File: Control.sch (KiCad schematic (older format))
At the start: 25 parts, among them J3 PDI, U6 ADR380, U7 ATXMEGA32E5-AU

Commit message: First working version
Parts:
- removed DS1: CV, smd-semi:LED-0603, symbol LED-0603
- removed DS2: CC, smd-semi:LED-0603, symbol LED-0603
- removed R52: 20k, IPC7351-Nominal:RESC1608X50, symbol R-0603
- removed W3: NET-TIE, conn-test:NET-TIE-1mm, symbol NET-TIE
- added C52, C53: 100n, IPC7351-Nominal:CAPC1608X55, symbol C-0603
- added DS1: CV, pth-semi:LED-5mm, symbol LED-5MM
- added DS2: CC, pth-semi:LED-5mm, symbol LED-5MM
- added J7: BUTTONS, conn-100mil:CONN-100MIL-M-1x3-SHROUD, symbol CONN-100MIL-M-1x3-SHROUD
- added U4: MCP9701-E/TO, conn-100mil:CONN-100MIL-M-1x3, symbol MCP9701-E/TO
- R32, R33, R56: value 330 -> 348; BOM RES SMD 330 1% [0603] -> RES SMD 348 1% [0603]
- R34, R50, R53: value 20k -> 22k; BOM RES SMD 20k 1% [0603] -> RES SMD 22k 1% [0603]
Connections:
- net labels added: PWR, TEMP, ~EN, ~ILIM, ~VLIM
- net labels removed: ILIM, VLIM
- wire segments 85 -> 99
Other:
- note added: "Ratio: 1/12"
- moved on the sheet: C20, C21, C51, R32, R33, R50, R51, R54, R55

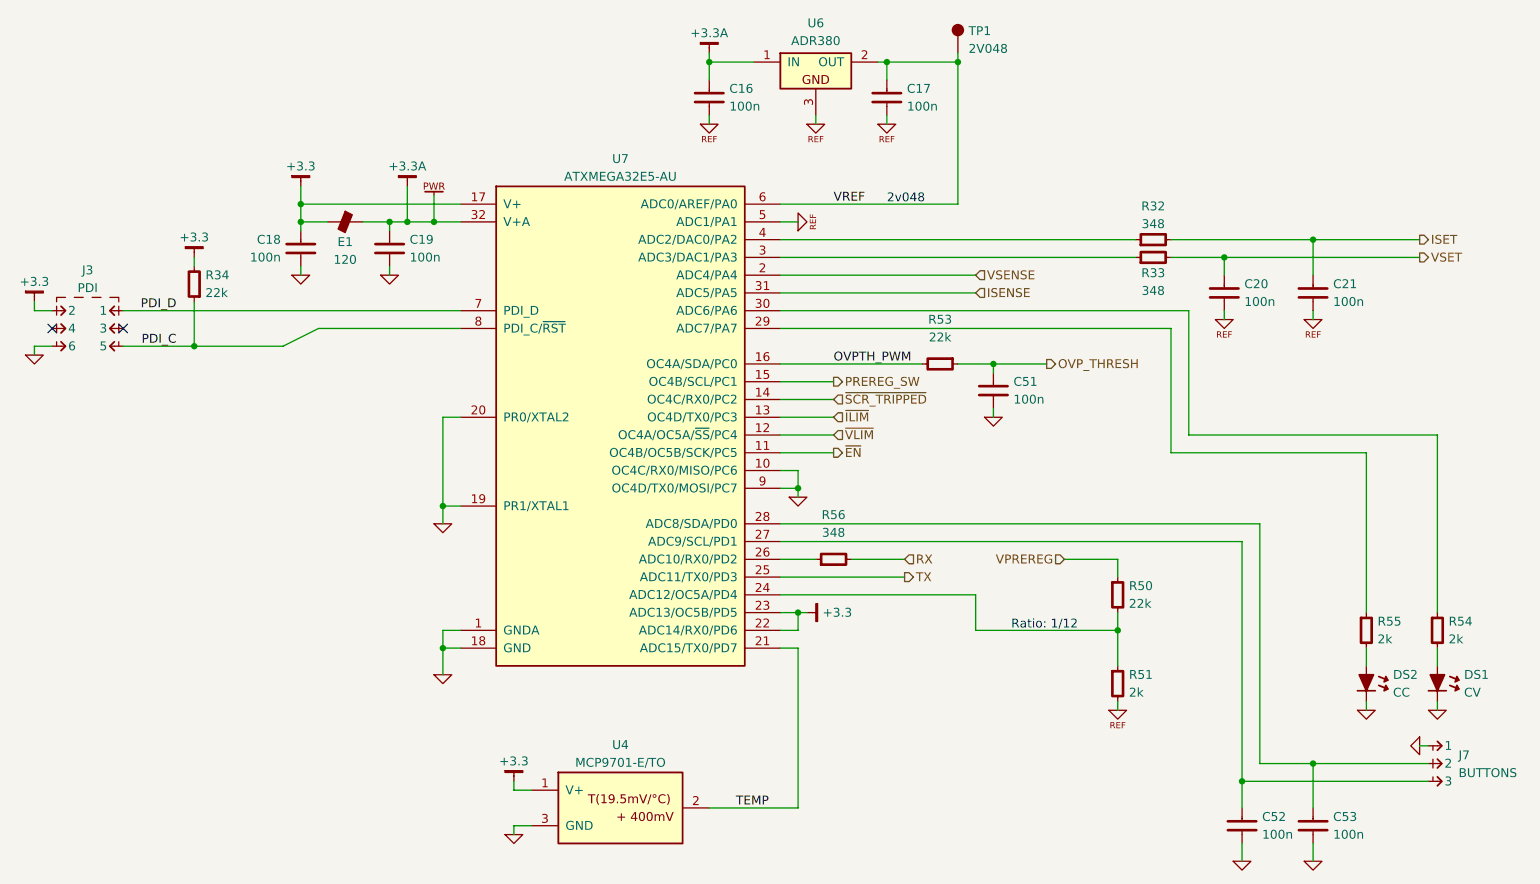
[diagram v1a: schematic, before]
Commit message: Reannotate component references
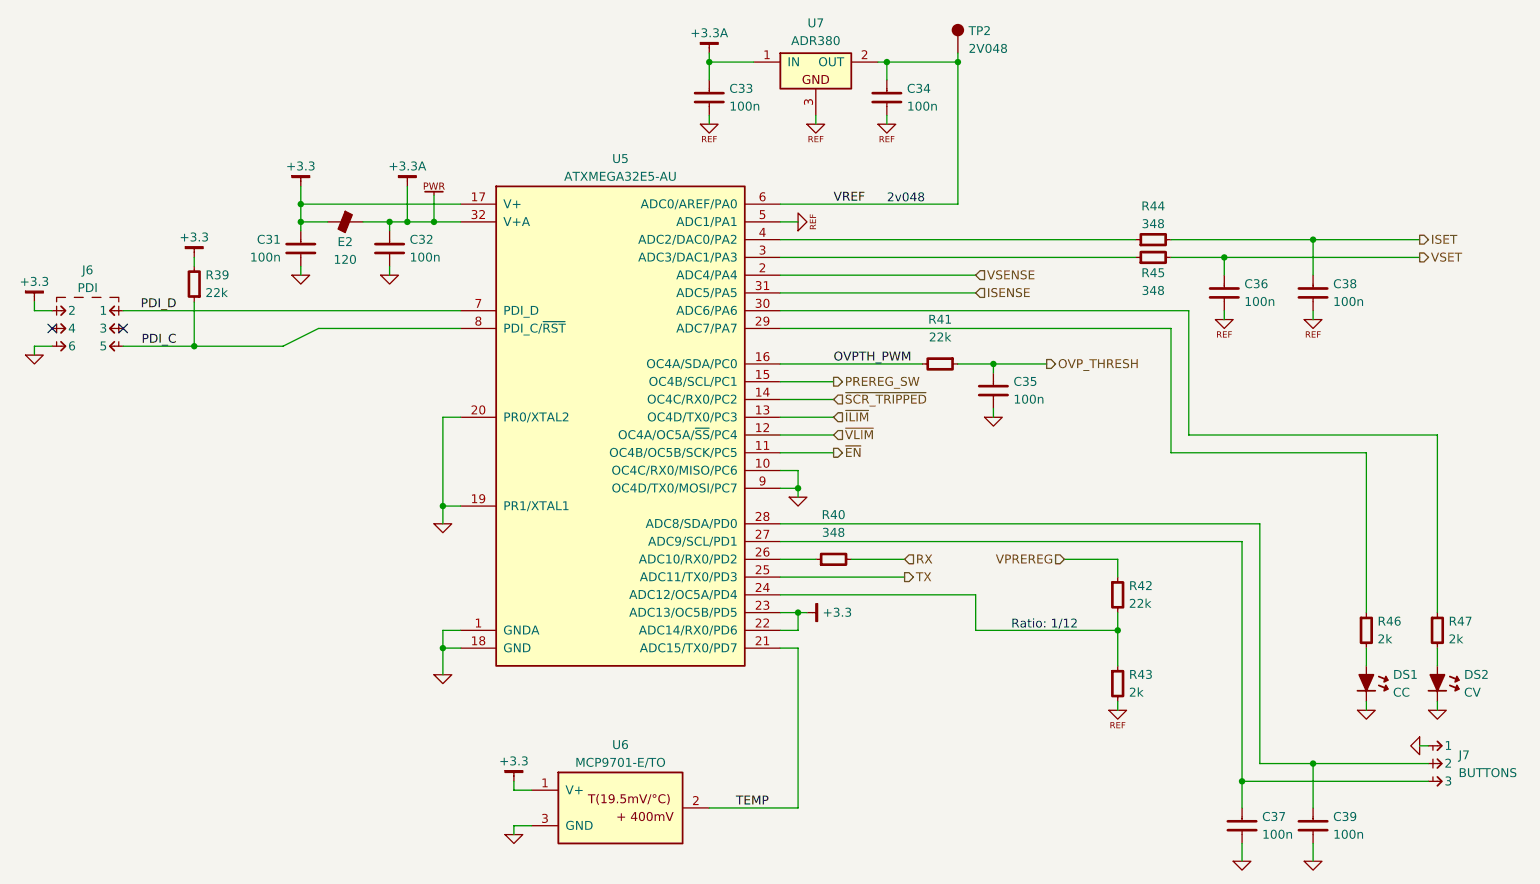
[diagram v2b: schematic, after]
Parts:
- renumbered C18 to C31, C19 to C32, C16 to C33, C17 to C34, C51 to C35, C20 to C36, C52 to C37, C21 to C38, C53 to C39, DS2 to DS1, DS1 to DS2, E1 to E2, J3 to J6, R34 to R39, R56 to R40, R53 to R41, R50 to R42, R51 to R43, R32 to R44, R33 to R45, R55 to R46, R54 to R47, TP1 to TP2, U7 to U5, U4 to U6, U6 to U7

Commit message: Piles and piles of work
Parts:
- removed R40: 348, IPC7351-Nominal:RESC1608X50, symbol R-0603
- removed U5: ATXMEGA32E5-AU, IPC7351-Nominal:QFP80P900X900X120-32, symbol ATXMEGA32E5-AU
- added U5: ATXMEGA8E5-AU, IPC7351-Nominal:QFP80P900X900X120-32, symbol ATXMEGA8E5-AU
- J6: BOM (none) -> (6) PIN STRIP 100mil
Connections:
- net +3.3: now also U5.17 (V+), U5.22 (ADC14/RX0/PD6), U5.23 (ADC13/OC5B/PD5)
- net +3.3A: now also U5.32 (V+A)
- net GND: now also U5.1 (GNDA), U5.10 (OC4C/RX0/MISO/PC6), U5.18 (GND), U5.19 (PR1/XTAL1), U5.20 (PR0/XTAL2), U5.9 (OC4D/TX0/MOSI/PC7)
- net ISENSE: now also U5.31 (ADC5/PA5)
- net OVPTH_PWM: now also U5.16 (OC4A/SDA/PC0)
- net PDI_C: now also U5.8 (PDI_C/~RST)
- net PDI_D: now also U5.7 (PDI_D)
- net PREREG_SW: now also U5.15 (OC4B/SCL/PC1)
- net REFGND: now also U5.5 (ADC1/PA1)
- net RX: now also U5.26 (ADC10/RX0/PD2)
- net TEMP: now also U5.21 (ADC15/TX0/PD7)
- net TX: now also U5.25 (ADC11/TX0/PD3)
- net VREF: now also U5.6 (ADC0/AREF/PA0)
- net VSENSE: now also U5.2 (ADC4/PA4)
- net ~EN: now also U5.11 (OC4B/OC5B/SCK/PC5)
- net ~ILIM: now also U5.13 (OC4D/TX0/PC3)
- net ~SCR_TRIPPED: now also U5.14 (OC4C/RX0/PC2)
- net ~VLIM: now also U5.12 (OC4A/OC5A/~SS~/PC4)
- net at R42.2, R43.1: now also U5.24 (ADC12/OC5A/PD4)
- net at C37.2, J7.3: now also U5.27 (ADC9/SCL/PD1)
- net at C39.2, J7.2: now also U5.28 (ADC8/SDA/PD0)
- net at R46.1: now also U5.29 (ADC7/PA7)
- net at R45.1: now also U5.3 (ADC3/DAC1/PA3)
- net at R47.1: now also U5.30 (ADC6/PA6)
- net at R44.1: now also U5.4 (ADC2/DAC0/PA2)
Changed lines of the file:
@@
 $EndDescr
 $Comp
-L ATXMEGA32E5-AU U5
-U 1 1 55CC4ECA
-P 4500 3950
-F 0 "U5" H 4500 5455 50  0000 C CNN
-F 1 "ATXMEGA32E5-AU" H 4500 5355 50  0000 C CNN
-F 2 "IPC7351-Nominal:QFP80P900X900X120-32" H 4500 2550 50  0001 C CNN
-F 3 "" H 4200 4300 50  0000 C CNN
-F 4 "IC ATMEL ATXMEGA32E5-AU" H 4500 2450 50  0001 C CNN "BOM"
-	1    4500 3950
-	1    0    0    -1
-$EndComp
-$Comp
-L +3.3 #PWR67
+L +3.3 #PWR66
 U 1 1 55CC5274
 P 2700 2600
-F 0 "#PWR67" H 2700 2650 30  0001 C CNN
+F 0 "#PWR66" H 2700 2650 30  0001 C CNN
 F 1 "+3.3" H 2700 2713 50  0000 C CNN
 F 2 "" H 2700 2600 60  0000 C CNN
@@
 $EndComp
 $Comp
-L GND #PWR68
+L GND #PWR67
 U 1 1 55CCA52E
 P 2700 3100
-F 0 "#PWR68" H 2700 3100 30  0001 C CNN
+F 0 "#PWR67" H 2700 3100 30  0001 C CNN
 F 1 "GND" H 2700 3030 30  0001 C CNN
 F 2 "" H 2700 3100 60  0000 C CNN
@@
 $EndComp
 $Comp
-L GND #PWR73
+L GND #PWR72
 U 1 1 55CCA8CD
 P 3500 5350
-F 0 "#PWR73" H 3500 5350 30  0001 C CNN
+F 0 "#PWR72" H 3500 5350 30  0001 C CNN
 F 1 "GND" H 3500 5280 30  0001 C CNN
 F 2 "" H 3500 5350 60  0000 C CNN
@@
 $EndComp
 $Comp
-L +3.3A #PWR76
+L +3.3A #PWR75
 U 1 1 55CCD224
 P 5000 1850
-F 0 "#PWR76" H 5000 1900 30  0001 C CNN
+F 0 "#PWR75" H 5000 1900 30  0001 C CNN
 F 1 "+3.3A" H 5000 1963 50  0000 C CNN
 F 2 "" H 5000 1850 60  0000 C CNN
@@
 $EndComp
 $Comp
-L +3.3A #PWR70
+L +3.3A #PWR69
 U 1 1 55CCD672
 P 3300 2600
-F 0 "#PWR70" H 3300 2650 30  0001 C CNN
+F 0 "#PWR69" H 3300 2650 30  0001 C CNN
 F 1 "+3.3A" H 3300 2713 50  0000 C CNN
 F 2 "" H 3300 2600 60  0000 C CNN
@@
 F 2 "conn-100mil:CONN-100MIL-M-2x3" H 1475 3300 50  0001 C CNN
 F 3 "" H 1475 3300 50  0000 C CNN
+F 4 "(6) PIN STRIP 100mil" H 1500 3300 60  0001 C CNN "BOM"
 	1    1500 3300
 	-1   0    0    -1
@@
 NoConn ~ 1300 3400
 $Comp
-L +3.3 #PWR64
+L +3.3 #PWR63
 U 1 1 55CD2985
 P 1200 3250
-F 0 "#PWR64" H 1200 3300 30  0001 C CNN
+F 0 "#PWR63" H 1200 3300 30  0001 C CNN
 F 1 "+3.3" H 1200 3363 50  0000 C CNN
 F 2 "" H 1200 3250 60  0000 C CNN
@@
 $EndComp
 $Comp
-L GND #PWR65
+L GND #PWR64
 U 1 1 55CD29EB
 P 1200 3550
-F 0 "#PWR65" H 1200 3550 30  0001 C CNN
+F 0 "#PWR64" H 1200 3550 30  0001 C CNN
 F 1 "GND" H 1200 3480 30  0001 C CNN
 F 2 "" H 1200 3550 60  0000 C CNN
@@
 $EndComp
 $Comp
-L +3.3 #PWR66
+L +3.3 #PWR65
 U 1 1 55CD3055
 P 2100 3000
-F 0 "#PWR66" H 2100 3050 30  0001 C CNN
+F 0 "#PWR65" H 2100 3050 30  0001 C CNN
 F 1 "+3.3" H 2100 3113 50  0000 C CNN
 F 2 "" H 2100 3000 60  0000 C CNN
@@
 RX
 $Comp
-L REFGND #PWR82
+L REFGND #PWR81
 U 1 1 55D1DEF0
 P 6000 2250
-F 0 "#PWR82" H 6000 2250 30  0001 C CNN
+F 0 "#PWR81" H 6000 2250 30  0001 C CNN
 F 1 "REFGND" H 6000 2180 30  0001 C CNN
 F 2 "" H 6000 2250 60  0000 C CNN
@@
 $EndComp
 $Comp
-L REFGND #PWR81
+L REFGND #PWR80
 U 1 1 55D1DF25
 P 5600 2250
-F 0 "#PWR81" H 5600 2250 30  0001 C CNN
+F 0 "#PWR80" H 5600 2250 30  0001 C CNN
 F 1 "REFGND" H 5600 2180 30  0001 C CNN
 F 2 "" H 5600 2250 60  0000 C CNN
@@
 $EndComp
 $Comp
-L REFGND #PWR77
+L REFGND #PWR76
 U 1 1 55D1DF5A
 P 5000 2250
-F 0 "#PWR77" H 5000 2250 30  0001 C CNN
+F 0 "#PWR76" H 5000 2250 30  0001 C CNN
 F 1 "REFGND" H 5000 2180 30  0001 C CNN
 F 2 "" H 5000 2250 60  0000 C CNN
@@
 ISENSE
 $Comp
-L REFGND #PWR85
+L REFGND #PWR84
 U 1 1 55D23537
 P 7900 3350
-F 0 "#PWR85" H 7900 3350 30  0001 C CNN
+F 0 "#PWR84" H 7900 3350 30  0001 C CNN
 F 1 "REFGND" H 7900 3280 30  0001 C CNN
 F 2 "" H 7900 3350 60  0000 C CNN
@@
 $EndComp
 $Comp
-L REFGND #PWR87
+L REFGND #PWR86
 U 1 1 55D235A7
 P 8400 3350
-F 0 "#PWR87" H 8400 3350 30  0001 C CNN
+F 0 "#PWR86" H 8400 3350 30  0001 C CNN
 F 1 "REFGND" H 8400 3280 30  0001 C CNN
 F 2 "" H 8400 3350 60  0000 C CNN
@@
 $EndComp
 $Comp
-L REFGND #PWR84
+L REFGND #PWR83
 U 1 1 55D18E16
 P 7300 5550
-F 0 "#PWR84" H 7300 5550 30  0001 C CNN
+F 0 "#PWR83" H 7300 5550 30  0001 C CNN
 F 1 "REFGND" H 7300 5480 30  0001 C CNN
 F 2 "" H 7300 5550 60  0000 C CNN
@@
 $EndComp
 $Comp
-L GND #PWR83
+L GND #PWR82
 U 1 1 55D1B336
 P 6600 3900
-F 0 "#PWR83" H 6600 3900 30  0001 C CNN
+F 0 "#PWR82" H 6600 3900 30  0001 C CNN
 F 1 "GND" H 6600 3830 30  0001 C CNN
 F 2 "" H 6600 3900 60  0000 C CNN
@@
 $EndComp
 $Comp
-L GND #PWR91
+L GND #PWR90
 U 1 1 55D18733
 P 9100 5550
-F 0 "#PWR91" H 9100 5550 30  0001 C CNN
+F 0 "#PWR90" H 9100 5550 30  0001 C CNN
 F 1 "GND" H 9100 5480 30  0001 C CNN
 F 2 "" H 9100 5550 60  0000 C CNN
@@
 $EndComp
 $Comp
-L GND #PWR89
+L GND #PWR88
 U 1 1 55D18843
 P 8700 5550
-F 0 "#PWR89" H 8700 5550 30  0001 C CNN
+F 0 "#PWR88" H 8700 5550 30  0001 C CNN
 F 1 "GND" H 8700 5480 30  0001 C CNN
 F 2 "" H 8700 5550 60  0000 C CNN
@@
 	1    8700 5550
 	1    0    0    -1
-$EndComp
-$Comp
-L R-0603 R?
-U 1 1 55D19211
-P 5700 4700
-AR Path="/55C7FF09/55D19211" Ref="R?"  Part="1"
-AR Path="/55CDE77D/55D19211" Ref="R40"  Part="1"
-F 0 "R40" V 5950 4700 50  0000 C CNN
-F 1 "348" V 5850 4700 50  0000 C CNN
-F 2 "IPC7351-Nominal:RESC1608X50" H 5700 4700 50  0001 C CNN
-F 3 "" H 5700 4750 60  0000 C CNN
-F 4 "RES SMD 348 1% [0603]" H 6450 5250 60  0001 C CNN "BOM"
-	1    5700 4700
-	0    -1   -1   0
 $EndComp
 $Comp
@@
 $EndComp
 $Comp
-L GND #PWR72
+L GND #PWR71
 U 1 1 55D1CF59
 P 3500 4500
-F 0 "#PWR72" H 3500 4500 30  0001 C CNN
+F 0 "#PWR71" H 3500 4500 30  0001 C CNN
 F 1 "GND" H 3500 4430 30  0001 C CNN
 F 2 "" H 3500 4500 60  0000 C CNN
@@
 $EndComp
 $Comp
-L REFGND #PWR78
+L REFGND #PWR77
 U 1 1 55D2A12D
 P 5500 2800
-F 0 "#PWR78" H 5500 2800 30  0001 C CNN
+F 0 "#PWR77" H 5500 2800 30  0001 C CNN
 F 1 "REFGND" H 5500 2730 30  0001 C CNN
 F 2 "" H 5500 2800 60  0000 C CNN
@@
 $EndComp
 $Comp
-L GND #PWR90
+L GND #PWR89
 U 1 1 55D2D2D5
 P 9000 5750
-F 0 "#PWR90" H 9000 5750 30  0001 C CNN
+F 0 "#PWR89" H 9000 5750 30  0001 C CNN
 F 1 "GND" H 9000 5680 30  0001 C CNN
 F 2 "" H 9000 5750 60  0000 C CNN
@@
 $EndComp
 $Comp
-L GND #PWR88
+L GND #PWR87
 U 1 1 55D2DDFE
 P 8400 6400
-F 0 "#PWR88" H 8400 6400 30  0001 C CNN
+F 0 "#PWR87" H 8400 6400 30  0001 C CNN
 F 1 "GND" H 8400 6330 30  0001 C CNN
 F 2 "" H 8400 6400 60  0000 C CNN
@@
 $EndComp
 $Comp
-L GND #PWR86
+L GND #PWR85
 U 1 1 55D2DEEC
 P 8000 6400
-F 0 "#PWR86" H 8000 6400 30  0001 C CNN
+F 0 "#PWR85" H 8000 6400 30  0001 C CNN
 F 1 "GND" H 8000 6330 30  0001 C CNN
 F 2 "" H 8000 6400 60  0000 C CNN
@@
 $EndComp
 $Comp
-L GND #PWR69
+L GND #PWR68
 U 1 1 55D3FD38
 P 3200 3100
-F 0 "#PWR69" H 3200 3100 30  0001 C CNN
+F 0 "#PWR68" H 3200 3100 30  0001 C CNN
 F 1 "GND" H 3200 3030 30  0001 C CNN
 F 2 "" H 3200 3100 60  0000 C CNN
@@
 ~EN
 $Comp
-L GND #PWR79
+L GND #PWR78
 U 1 1 55D43492
 P 5500 4350
-F 0 "#PWR79" H 5500 4350 30  0001 C CNN
+F 0 "#PWR78" H 5500 4350 30  0001 C CNN
 F 1 "GND" H 5500 4280 30  0001 C CNN
 F 2 "" H 5500 4350 60  0000 C CNN
@@
 $EndComp
 $Comp
-L +3.3 #PWR80
+L +3.3 #PWR79
 U 1 1 55D43F25
 P 5550 5000
-F 0 "#PWR80" H 5550 5050 30  0001 C CNN
+F 0 "#PWR79" H 5550 5050 30  0001 C CNN
 F 1 "+3.3" V 5550 5088 50  0000 L CNN
 F 2 "" H 5550 5000 60  0000 C CNN
@@
 	8700 4100 8700 5000
 Wire Wire Line
-	5800 4700 6100 4700
-Wire Wire Line
-	5600 4700 5400 4700
+	5400 4700 6100 4700
 Connection ~ 6400 1900
 Wire Wire Line
@@
 	7400 3000 5400 3000
 $Comp
-L PWR #PWR71
+L PWR #PWR70
 U 1 1 55D3F3A8
 P 3450 2650
-F 0 "#PWR71" H 3450 2650 50  0001 C CNN
+F 0 "#PWR70" H 3450 2650 50  0001 C CNN
 F 1 "PWR" H 3450 2650 50  0001 C CNN
 F 2 "" H 3450 2650 60  0000 C CNN
@@
 $EndComp
 $Comp
-L +3.3 #PWR74
+L +3.3 #PWR73
 U 1 1 55D693B1
 P 3900 5950
-F 0 "#PWR74" H 3900 6000 30  0001 C CNN
+F 0 "#PWR73" H 3900 6000 30  0001 C CNN
 F 1 "+3.3" H 3900 6063 50  0000 C CNN
 F 2 "" H 3900 5950 60  0000 C CNN
@@
 	3900 6000 4000 6000
 $Comp
-L GND #PWR75
+L GND #PWR74
 U 1 1 55D69508
 P 3900 6250
-F 0 "#PWR75" H 3900 6250 30  0001 C CNN
+F 0 "#PWR74" H 3900 6250 30  0001 C CNN
 F 1 "GND" H 3900 6180 30  0001 C CNN
 F 2 "" H 3900 6250 60  0000 C CNN
@@
 Text Label 5150 6100 0    50   ~ 0
 TEMP
+$Comp
+L ATXMEGA8E5-AU U5
+U 1 1 55DC009F
+P 4500 3950
+F 0 "U5" H 4500 5455 50  0000 C CNN
+F 1 "ATXMEGA8E5-AU" H 4500 5355 50  0000 C CNN
+F 2 "IPC7351-Nominal:QFP80P900X900X120-32" H 4500 2550 50  0001 C CNN
+F 3 "" H 4200 4300 50  0000 C CNN
+F 4 "IC ATMEL ATXMEGA8E5-AU" H 4500 2450 50  0001 C CNN "BOM"
+	1    4500 3950
+	1    0    0    -1
+$EndComp
 $EndSCHEMATC
